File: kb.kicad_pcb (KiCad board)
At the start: 2 copper layers, 203.2 x 114.3 mm, 188 parts, among them J1 Conn_02x04, J2 10029449-001RLF, J3 Conn_01x05, J4 Conn_01x10, J5 Conn_01x07, J6 Conn_01x06, SW1 RotaryEncoder_Switch, U1 Pico, U2 SN74AHCT125D

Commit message: add new level shifter, add component values
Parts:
- added C45: 0.1uF, Capacitor_SMD:C_0805_2012Metric_Pad1.18x1.45mm_HandSolder, B.Cu at (42.9, 62.0)
- added C46: 0.1uF, Capacitor_SMD:C_0805_2012Metric_Pad1.18x1.45mm_HandSolder, B.Cu at (45.5, 70.2)
- R1, R2: value R_Small_US -> 4.7k
- U2: value SN74AHCT125D -> TXB0101DBVR; footprint Package_SO:TSSOP-14-1EP_4.4x5mm_P0.65mm -> TXB0101DBVR:SOT65P210X110-6N
- moved U2 2.77 mm to (44.5, 65.9)
- moved D0 1.59 mm to (42.9, 70.6)
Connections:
- U2 pad 1: GND -> +3V3
- U2 pad 3: unconnected-(U2-Pad3) -> /RGB_3V3
- U2 pad 4: GND -> /RGB_5V
- U2 pad 5: GND -> +3V3
- U2 pad 6: unconnected-(U2-Pad6) -> +5V
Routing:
- net GND: track 25.7 -> 12.7 mm, vias 173 -> 174
- net +3V3: track 75.2 -> 87.8 mm, vias 0 -> 1
- net +5V: track 1119.0 -> 1116.1 mm
- net /RGB_3V3: track 14.1 -> 11.6 mm
- net Net-(D0-Pad2): track 22.2 -> 20.6 mm
- net /ROW0: track 249.7 -> 251.2 mm
- net /RGB_5V: track 24.8 -> 26.1 mm

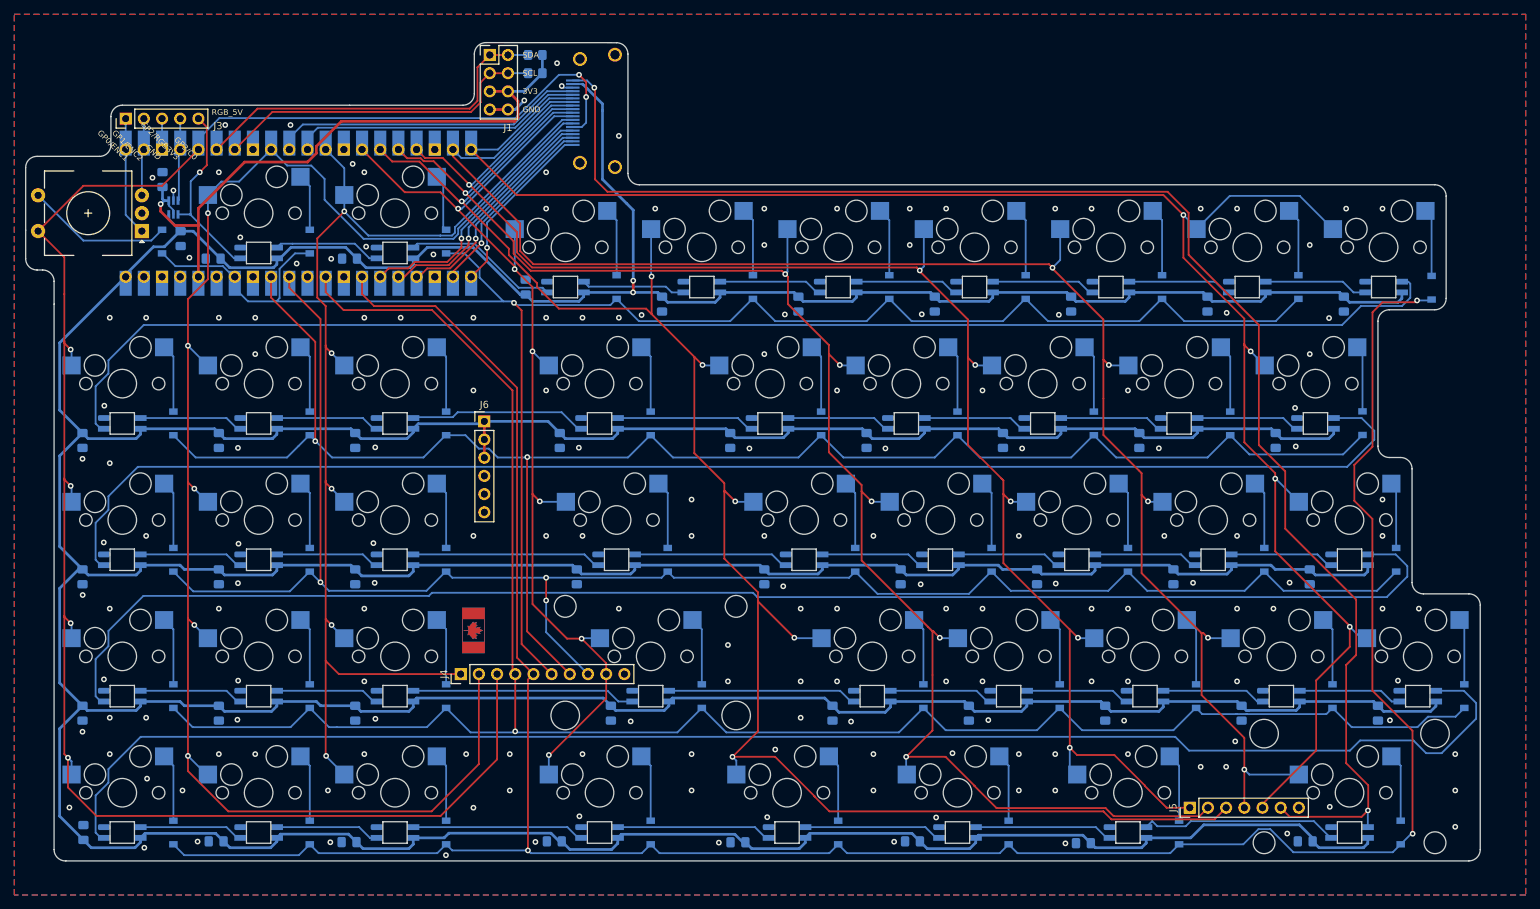
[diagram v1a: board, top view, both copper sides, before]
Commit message: changed footprints
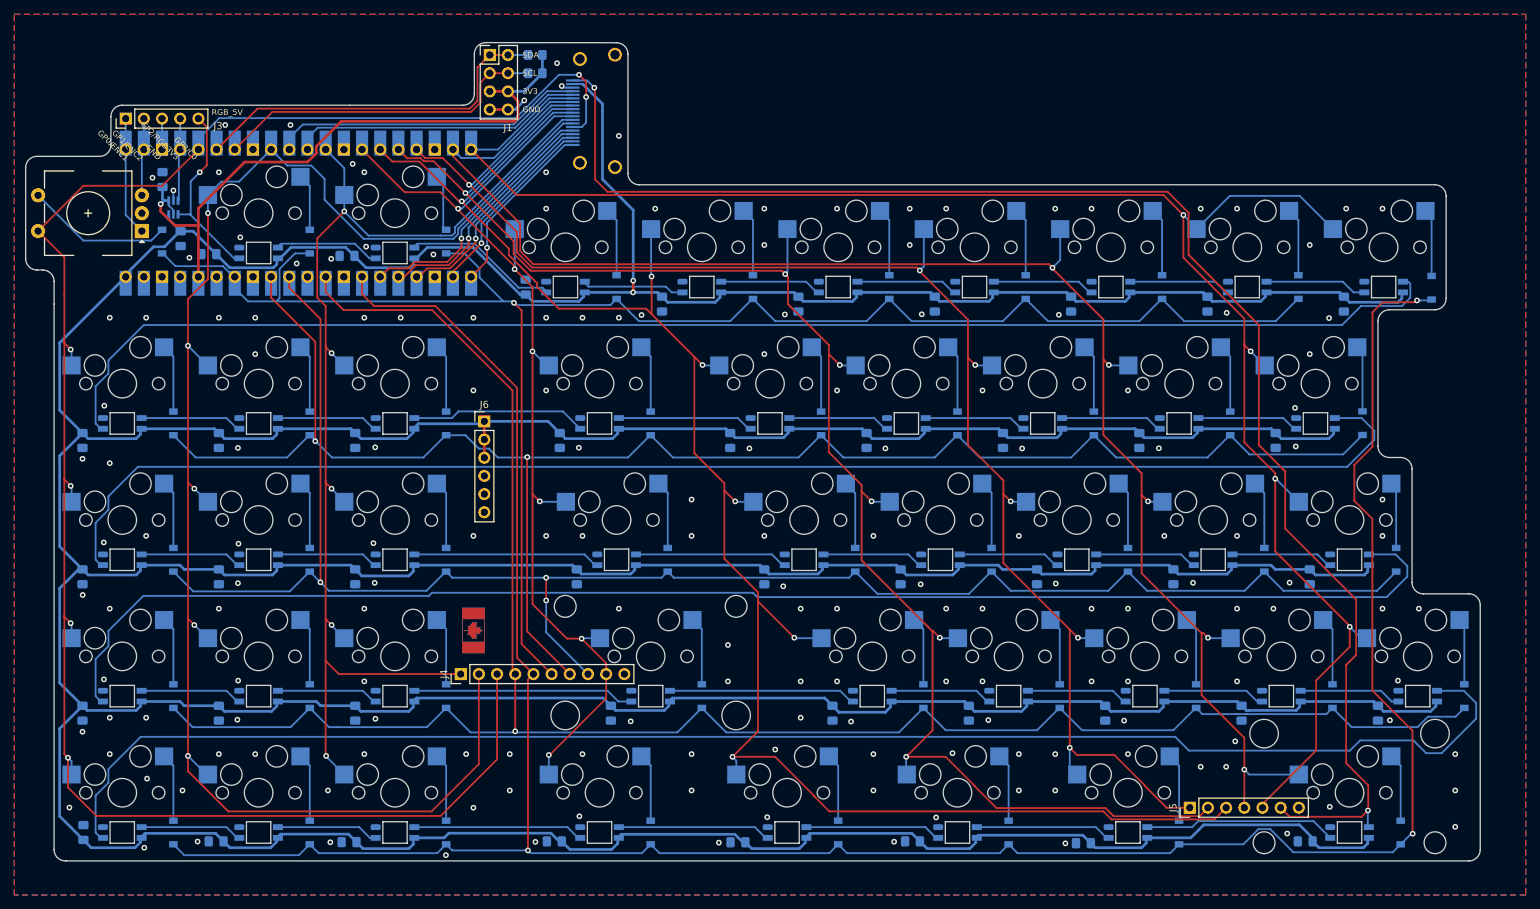
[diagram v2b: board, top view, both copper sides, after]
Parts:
- moved C1 0.88 mm to (49.4, 72.4)
- moved C2 0.52 mm to (68.7, 72.6)
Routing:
- net Net-(D142-Pad2): track 27.8 -> 26.9 mm

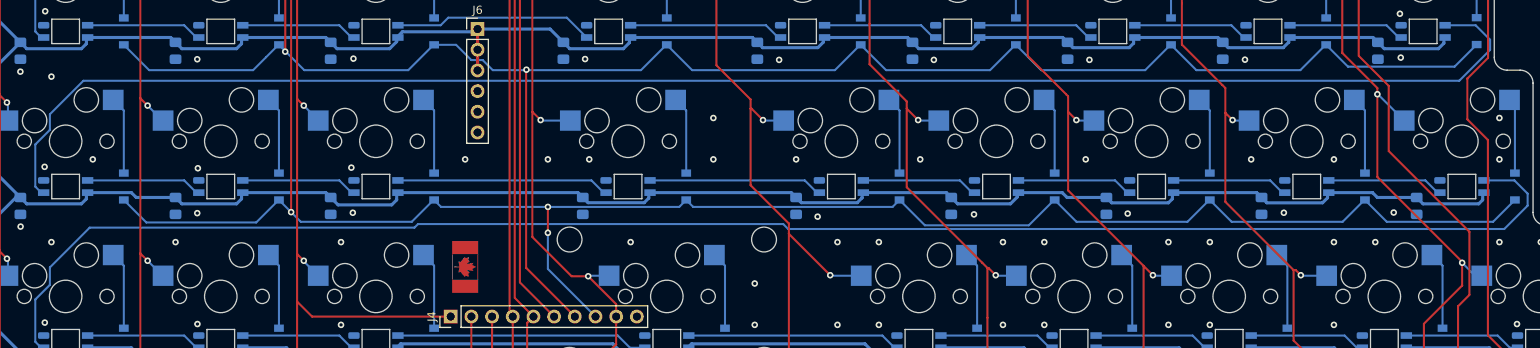
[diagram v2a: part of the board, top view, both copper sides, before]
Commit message: added stepped capslock support
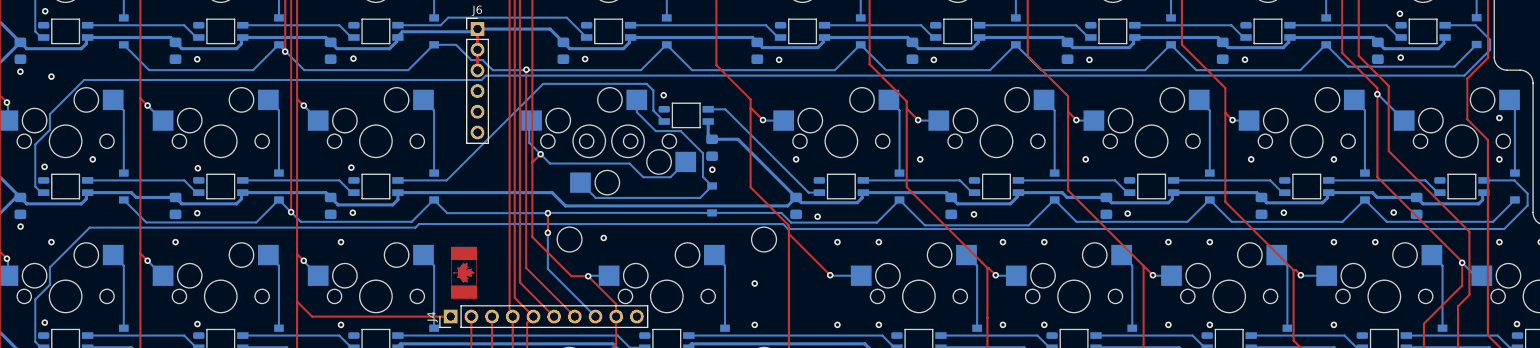
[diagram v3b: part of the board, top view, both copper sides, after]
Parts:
- added MX21_1: MX-NoLED, MX_Only:MXOnly-1.25U-Hotswap, F.Cu at (101.6, 109.5)
- C1, C10, C11, C12, C13, C14, C15, C16, C17, C18, C19, C2, C20, C21, C22, C23, C24, C25, C26, C27, C28, C29, C3, C30, C31, C32, C33, C34, C35, C36, C37, C38, C39, C4, C40, C41, C42, C43, C44, C5, C6, C7, C8, C9: value C_Small -> 0.1uF
- moved C21 17.4 mm to (116.7, 110.3)
- moved D121 11.3 mm to (113.5, 106.4)
- moved D21 3.55 mm to (116.7, 116.7)
- turned MX21 to 180 degrees
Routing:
- net Net-(D21-Pad2): track 9.53 -> 33.7 mm
- net /COL3: track 146.8 -> 167.7 mm
- net +5V: track 1116.1 -> 1131.2 mm
- net Net-(D120-Pad2): track 26.5 -> 41.0 mm
- net Net-(D121-Pad2): track 21.7 -> 17.9 mm
- net GND: vias 174 -> 171
